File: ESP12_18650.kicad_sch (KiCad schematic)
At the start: 28 parts, among them J1 Conn_02x06_Counter_Clockwise, J10 Conn_01x06_Male, J11 Conn_01x06_Male, J12 Conn_01x06_Male, J13 Conn_01x06_Male, J14 Conn_01x06_Male, J15 Conn_01x06_Male, J16 Conn_01x06_Male, J17 Conn_01x14_Male, J2 Conn_01x14_Male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

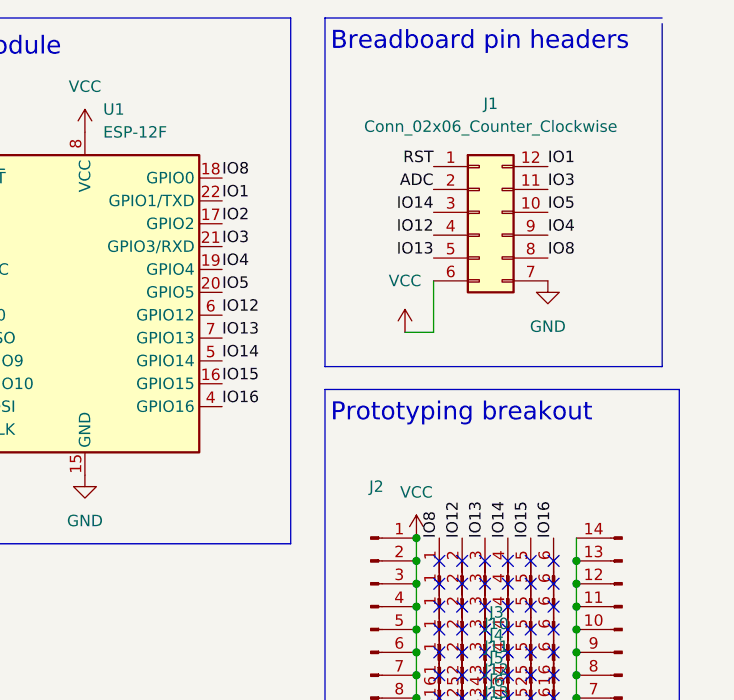
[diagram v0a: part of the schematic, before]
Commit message: Fix netname and silkscreen for GPIO 0
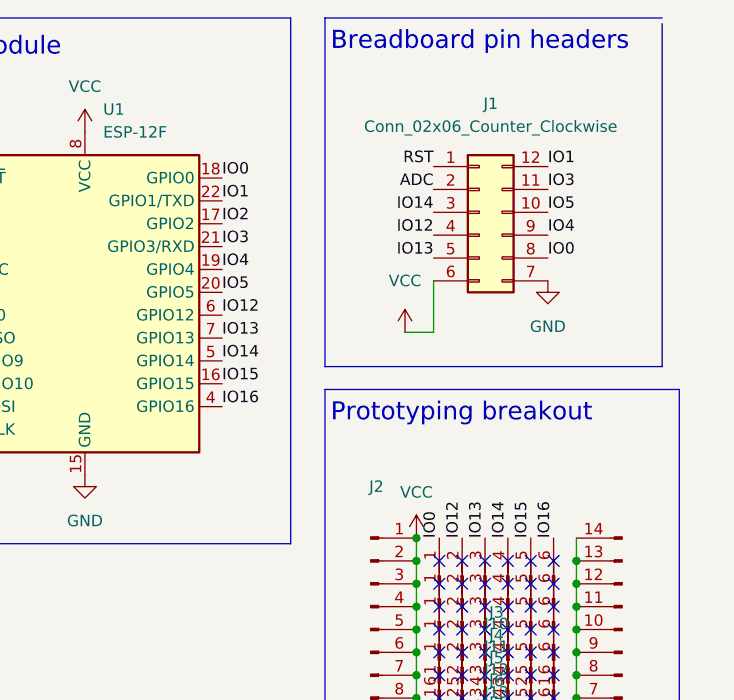
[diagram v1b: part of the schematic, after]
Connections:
- net IO8 renamed IO0
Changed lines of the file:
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@@
     (effects (font (size 1.27 1.27)) (justify right bottom))
   )
-  (label "IO8" (at 140.335 78.74 90)
+  (label "IO0" (at 140.335 78.74 90)
     (effects (font (size 1.27 1.27)) (justify left bottom))
   )
@@
     (effects (font (size 1.27 1.27)) (justify right bottom))
   )
-  (label "IO8" (at 116.205 38.735 0)
+  (label "IO0" (at 116.205 38.735 0)
     (effects (font (size 1.27 1.27)) (justify left bottom))
   )
@@
     (effects (font (size 1.27 1.27)) (justify right bottom))
   )
-  (label "IO8" (at 152.4 47.625 0)
+  (label "IO0" (at 152.4 47.625 0)
     (effects (font (size 1.27 1.27)) (justify left bottom))
   )

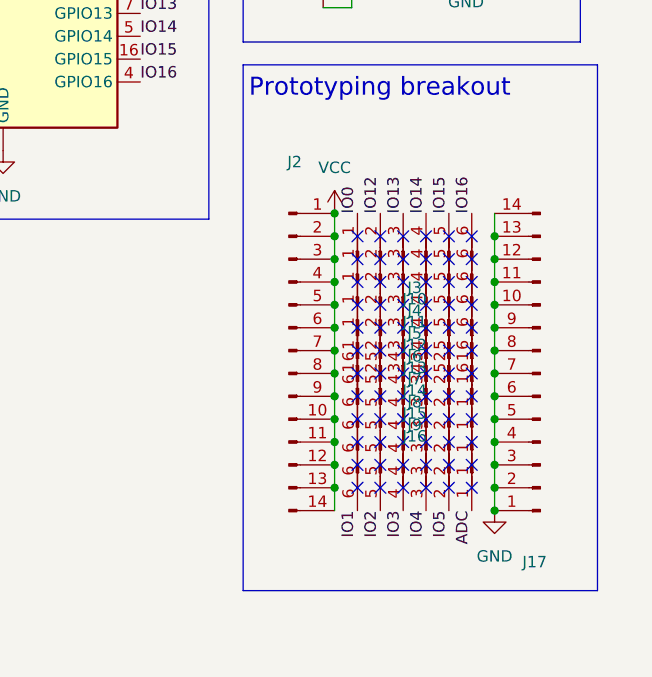
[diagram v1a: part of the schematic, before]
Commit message: Move IO0 to right side, and ADC to left
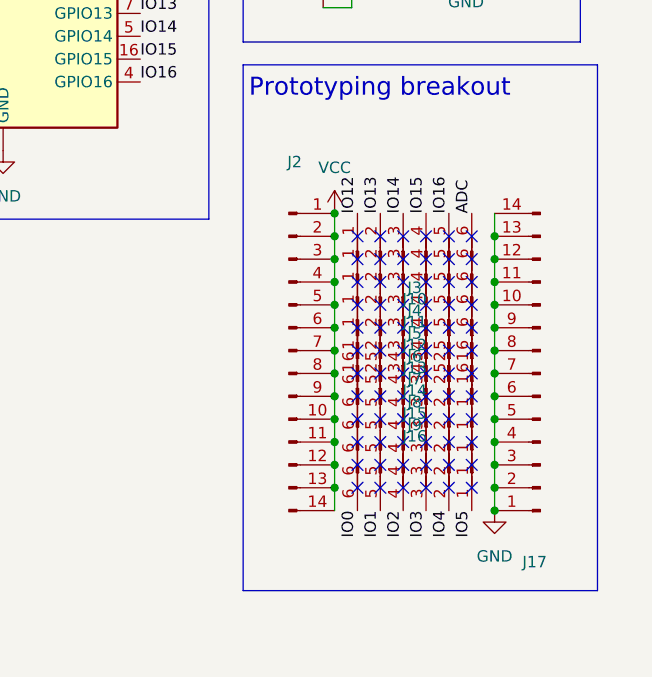
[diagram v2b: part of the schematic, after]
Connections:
- net ADC: now also J3.6 (Pin_6); no longer J16.1 (Pin_1)
- net IO0: now also J16.6 (Pin_6); no longer J3.1 (Pin_1)
- net IO1: now also J16.5 (Pin_5); no longer J16.6 (Pin_6)
- net IO12: now also J3.1 (Pin_1); no longer J3.2 (Pin_2)
- net IO13: now also J3.2 (Pin_2); no longer J3.3 (Pin_3)
- net IO14: now also J3.3 (Pin_3); no longer J3.4 (Pin_4)
- net IO15: now also J3.4 (Pin_4); no longer J3.5 (Pin_5)
- net IO16: now also J3.5 (Pin_5); no longer J3.6 (Pin_6)
- net IO2: now also J16.4 (Pin_4); no longer J16.5 (Pin_5)
- net IO3: now also J16.3 (Pin_3); no longer J16.4 (Pin_4)
- net IO4: now also J16.2 (Pin_2); no longer J16.3 (Pin_3)
- net IO5: now also J16.1 (Pin_1); no longer J16.2 (Pin_2)
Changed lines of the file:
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@@
     (effects (font (size 1.27 1.27)) (justify left bottom))
   )
-  (label "IO4" (at 147.955 111.76 270)
+  (label "IO4" (at 150.495 111.76 270)
     (effects (font (size 1.27 1.27)) (justify right bottom))
   )
@@
     (effects (font (size 1.27 1.27)) (justify left bottom))
   )
-  (label "IO2" (at 142.875 111.76 270)
+  (label "IO2" (at 145.415 111.76 270)
     (effects (font (size 1.27 1.27)) (justify right bottom))
   )
@@
     (effects (font (size 1.27 1.27)) (justify right bottom))
   )
-  (label "IO0" (at 140.335 78.74 90)
-    (effects (font (size 1.27 1.27)) (justify left bottom))
+  (label "IO0" (at 140.335 111.76 270)
+    (effects (font (size 1.27 1.27)) (justify right bottom))
   )
   (label "IO13" (at 139.7 47.625 180)
     (effects (font (size 1.27 1.27)) (justify right bottom))
   )
-  (label "IO12" (at 142.875 78.74 90)
+  (label "IO12" (at 140.335 78.74 90)
     (effects (font (size 1.27 1.27)) (justify left bottom))
   )
-  (label "IO14" (at 147.955 78.74 90)
+  (label "IO14" (at 145.415 78.74 90)
     (effects (font (size 1.27 1.27)) (justify left bottom))
   )
@@
     (effects (font (size 1.27 1.27)) (justify left bottom))
   )
-  (label "IO1" (at 140.335 111.76 270)
+  (label "IO1" (at 142.875 111.76 270)
     (effects (font (size 1.27 1.27)) (justify right bottom))
   )
@@
     (effects (font (size 1.27 1.27)) (justify right bottom))
   )
-  (label "IO16" (at 153.035 78.74 90)
+  (label "IO16" (at 150.495 78.74 90)
     (effects (font (size 1.27 1.27)) (justify left bottom))
   )
@@
     (effects (font (size 1.27 1.27)) (justify left bottom))
   )
-  (label "ADC" (at 153.035 111.76 270)
-    (effects (font (size 1.27 1.27)) (justify right bottom))
+  (label "ADC" (at 153.035 78.74 90)
+    (effects (font (size 1.27 1.27)) (justify left bottom))
   )
   (label "IO12" (at 139.7 45.085 180)
@@
     (effects (font (size 1.27 1.27)) (justify left bottom))
   )
-  (label "IO13" (at 145.415 78.74 90)
+  (label "IO13" (at 142.875 78.74 90)
     (effects (font (size 1.27 1.27)) (justify left bottom))
   )
@@
     (effects (font (size 1.27 1.27)) (justify left bottom))
   )
-  (label "IO5" (at 150.495 111.76 270)
+  (label "IO5" (at 153.035 111.76 270)
     (effects (font (size 1.27 1.27)) (justify right bottom))
   )
@@
     (effects (font (size 1.27 1.27)) (justify left bottom))
   )
-  (label "IO15" (at 150.495 78.74 90)
+  (label "IO15" (at 147.955 78.74 90)
     (effects (font (size 1.27 1.27)) (justify left bottom))
   )
@@
     (effects (font (size 1.27 1.27)) (justify left bottom))
   )
-  (label "IO3" (at 145.415 111.76 270)
+  (label "IO3" (at 147.955 111.76 270)
     (effects (font (size 1.27 1.27)) (justify right bottom))
   )
